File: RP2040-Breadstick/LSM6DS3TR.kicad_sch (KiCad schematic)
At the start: 2 parts, among them U401 LSM6DSMTR

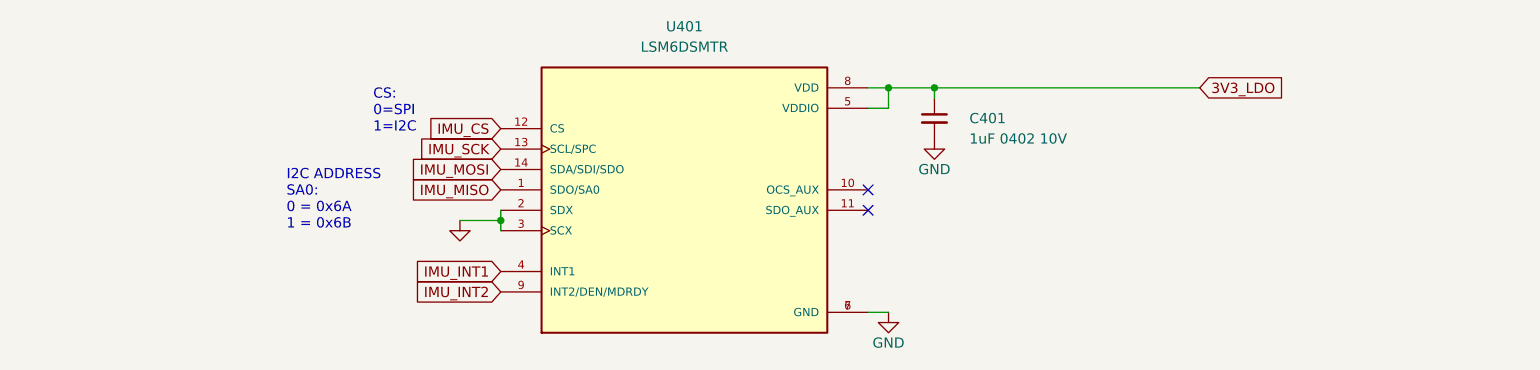
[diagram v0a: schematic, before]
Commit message: Switched IMU to I2C
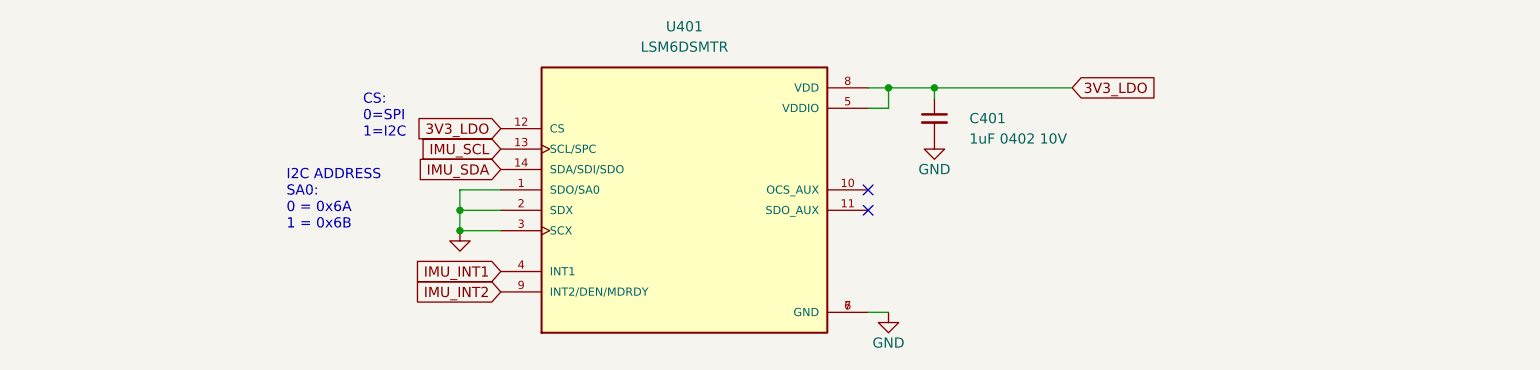
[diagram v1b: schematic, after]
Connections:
- net IMU_CS is gone; now on net 3V3_LDO: U401.12 (CS)
- net IMU_MISO is gone; now on net GND: U401.1 (SDO/SA0)
- net IMU_MOSI renamed IMU_SDA
- net IMU_SCK renamed IMU_SCL
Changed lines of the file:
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@@
   (junction (at 174.625 81.28) (diameter 0) (color 0 0 0 0)
   )
-  (junction (at 126.365 97.79) (diameter 0) (color 0 0 0 0)
+  (junction (at 121.285 99.06) (diameter 0) (color 0 0 0 0)
+  )
+  (junction (at 121.285 96.52) (diameter 0) (color 0 0 0 0)
   )
   (junction (at 180.34 81.28) (diameter 0) (color 0 0 0 0)
@@
     (stroke (width 0) (type default) (color 0 0 0 0))
   )
-  (wire (pts (xy 126.365 96.52) (xy 126.365 97.79))
+  (wire (pts (xy 121.285 93.98) (xy 121.285 96.52))
     (stroke (width 0) (type default) (color 0 0 0 0))
   )
-  (wire (pts (xy 126.365 97.79) (xy 126.365 99.06))
-    (stroke (width 0) (type default) (color 0 0 0 0))
-  )
-  (wire (pts (xy 180.34 81.28) (xy 213.36 81.28))
+  (wire (pts (xy 180.34 81.28) (xy 197.485 81.28))
     (stroke (width 0) (type default) (color 0 0 0 0))
   )
@@
     (stroke (width 0) (type default) (color 0 0 0 0))
   )
-  (wire (pts (xy 121.285 97.79) (xy 126.365 97.79))
+  (wire (pts (xy 174.625 83.82) (xy 174.625 81.28))
     (stroke (width 0) (type default) (color 0 0 0 0))
   )
-  (wire (pts (xy 174.625 83.82) (xy 174.625 81.28))
+  (wire (pts (xy 126.365 93.98) (xy 121.285 93.98))
     (stroke (width 0) (type default) (color 0 0 0 0))
   )
@@
     (stroke (width 0) (type default) (color 0 0 0 0))
   )
+  (wire (pts (xy 121.285 96.52) (xy 126.365 96.52))
+    (stroke (width 0) (type default) (color 0 0 0 0))
+  )
+  (wire (pts (xy 121.285 96.52) (xy 121.285 99.06))
+    (stroke (width 0) (type default) (color 0 0 0 0))
+  )
+  (wire (pts (xy 121.285 99.06) (xy 126.365 99.06))
+    (stroke (width 0) (type default) (color 0 0 0 0))
+  )
   (text "I2C ADDRESS\nSA0:\n0 = 0x6A\n1 = 0x6B" (at 99.695 99.06 0)
     (effects (font (size 1.27 1.27)) (justify left bottom))
   )
-  (text "CS:\n0=SPI\n1=I2C" (at 110.49 86.995 0)
+  (text "CS:\n0=SPI\n1=I2C" (at 109.22 87.63 0)
     (effects (font (size 1.27 1.27)) (justify left bottom))
   )
-  (global_label "IMU_SCK" (shape input) (at 126.365 88.9 180) (fields_autoplaced)
+  (global_label "IMU_SDA" (shape input) (at 126.365 91.44 180) (fields_autoplaced)
     (effects (font (size 1.27 1.27)) (justify right))
-    (property "Intersheet References" "${INTERSHEET_REFS}" (id 0) (at 115.8481 88.9794 0)
+    (property "Intersheet References" "${INTERSHEET_REFS}" (id 0) (at 116.0295 91.5194 0)
       (effects (font (size 1.27 1.27)) (justify right) hide)
     )
@@
     )
   )
-  (global_label "3V3_LDO" (shape input) (at 213.36 81.28 0) (fields_autoplaced)
+  (global_label "3V3_LDO" (shape input) (at 197.485 81.28 0) (fields_autoplaced)
     (effects (font (size 1.27 1.27)) (justify left))
-    (property "Intersheet References" "${INTERSHEET_REFS}" (id 0) (at 223.8769 81.2006 0)
+    (property "Intersheet References" "${INTERSHEET_REFS}" (id 0) (at 208.0019 81.2006 0)
       (effects (font (size 1.27 1.27)) (justify left) hide)
     )
@@
     )
   )
-  (global_label "IMU_CS" (shape input) (at 126.365 86.36 180) (fields_autoplaced)
+  (global_label "3V3_LDO" (shape input) (at 126.365 86.36 180) (fields_autoplaced)
     (effects (font (size 1.27 1.27)) (justify right))
-    (property "Intersheet References" "${INTERSHEET_REFS}" (id 0) (at 117.1181 86.4394 0)
+    (property "Intersheet References" "${INTERSHEET_REFS}" (id 0) (at 115.8481 86.4394 0)
       (effects (font (size 1.27 1.27)) (justify right) hide)
     )
   )
-  (global_label "IMU_MOSI" (shape input) (at 126.365 91.44 180) (fields_autoplaced)
+  (global_label "IMU_SCL" (shape input) (at 126.365 88.9 180) (fields_autoplaced)
     (effects (font (size 1.27 1.27)) (justify right))
-    (property "Intersheet References" "${INTERSHEET_REFS}" (id 0) (at 115.0014 91.5194 0)
-      (effects (font (size 1.27 1.27)) (justify right) hide)
-    )
-  )
-  (global_label "IMU_MISO" (shape input) (at 126.365 93.98 180) (fields_autoplaced)
-    (effects (font (size 1.27 1.27)) (justify right))
-    (property "Intersheet References" "${INTERSHEET_REFS}" (id 0) (at 115.0014 94.0594 0)
+    (property "Intersheet References" "${INTERSHEET_REFS}" (id 0) (at 116.09 88.9794 0)
       (effects (font (size 1.27 1.27)) (justify right) hide)
     )
@@
     (pin "1")
   )
-  (symbol (lib_id "power:GND") (at 121.285 97.79 0) (unit 1)
+  (symbol (lib_id "power:GND") (at 121.285 99.06 0) (unit 1)
     (in_bom yes) (on_board yes)
-    (property "Reference" "#PWR0401" (id 0) (at 121.285 104.14 0)
+    (property "Reference" "#PWR0401" (id 0) (at 121.285 105.41 0)
       (effects (font (size 1.27 1.27)) hide)
     )
-    (property "Value" "~" (id 1) (at 121.285 101.6 0))
-    (property "Footprint" "" (id 2) (at 121.285 97.79 0)
+    (property "Value" "~" (id 1) (at 121.285 102.87 0))
+    (property "Footprint" "" (id 2) (at 121.285 99.06 0)
       (effects (font (size 1.27 1.27)) hide)
     )
-    (property "Datasheet" "" (id 3) (at 121.285 97.79 0)
+    (property "Datasheet" "" (id 3) (at 121.285 99.06 0)
       (effects (font (size 1.27 1.27)) hide)
     )

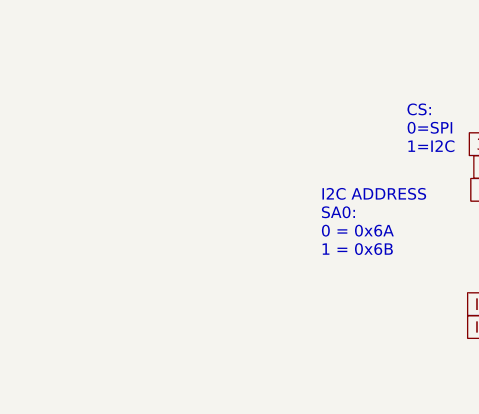
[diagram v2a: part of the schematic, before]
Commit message: Working on several issues simultaneously from the schematic side.
Added hierarchical connections between schematic sheets.
Added ideal ORing diodes.
Unstacked Pins and Added internal diagrams to: USB connector, TVS Diodes, ORing Diodes, LDO, RP2040, etc.
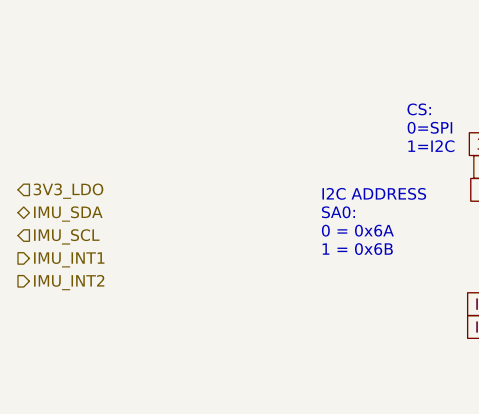
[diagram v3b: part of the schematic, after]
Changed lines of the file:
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@@
     )
+  )
+  (hierarchical_label "IMU_SCL" (shape input) (at 66.04 96.52 0)
+    (effects (font (size 1.27 1.27)) (justify left))
+  )
+  (hierarchical_label "IMU_INT2" (shape output) (at 66.04 101.6 0)
+    (effects (font (size 1.27 1.27)) (justify left))
+  )
+  (hierarchical_label "3V3_LDO" (shape input) (at 66.04 91.44 0)
+    (effects (font (size 1.27 1.27)) (justify left))
+  )
+  (hierarchical_label "IMU_SDA" (shape bidirectional) (at 66.04 93.98 0)
+    (effects (font (size 1.27 1.27)) (justify left))
+  )
+  (hierarchical_label "IMU_INT1" (shape output) (at 66.04 99.06 0)
+    (effects (font (size 1.27 1.27)) (justify left))
   )
   (symbol (lib_id "Device:C_Small") (at 180.34 85.09 0) (mirror y) (unit 1)

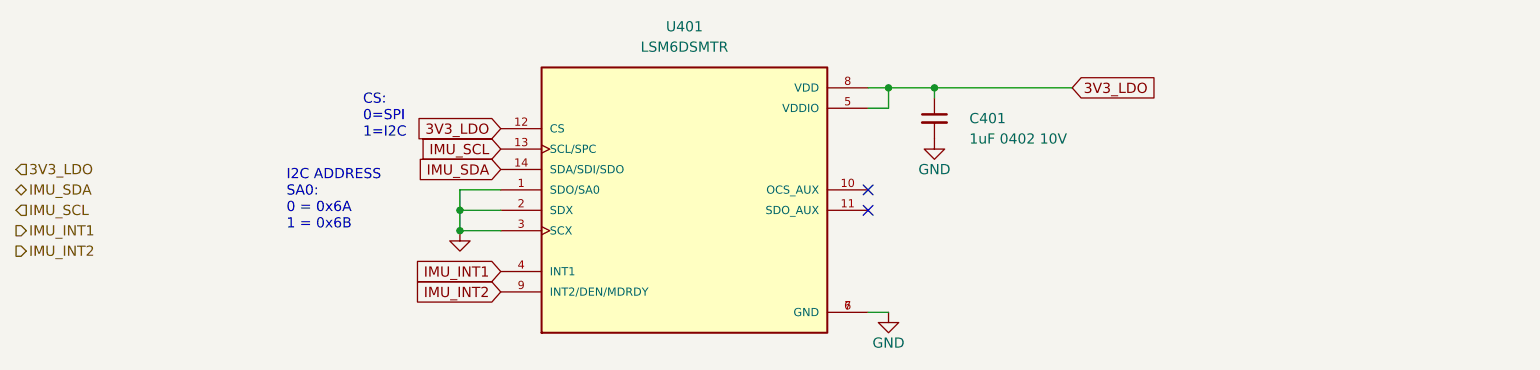
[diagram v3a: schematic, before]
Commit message: Continued cleaning up schematic
Finished most of the microcontroller sheet.
Added hierarchical pins to LED and IMU sheets.
Replaced 24 caps for the LEDs with 6 1206 caps.
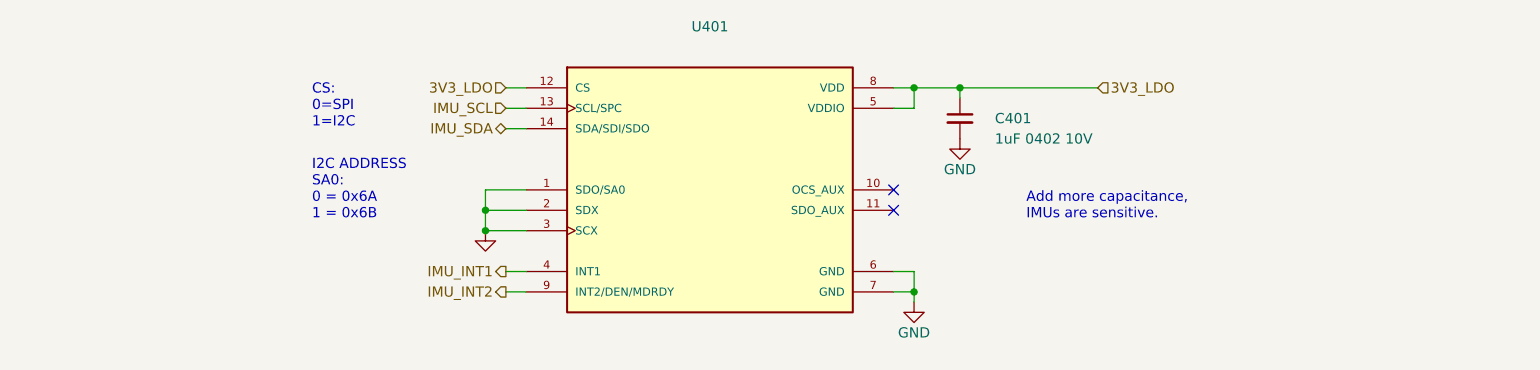
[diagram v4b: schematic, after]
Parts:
- U401: value LSM6DSMTR -> (none); footprint LSM6DSMTR:PQFN50P300X250X86-14N -> PQFN50P300X250X86-14N
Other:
- note added: "Add more capacitance, IMUs are sensitive."
- moved on the sheet: C401

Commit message: Moved schematic changes into PCB
All the changes made in the schematic have been moved into the PCB editor. It was a bit of work due to the amount of reorganizing done in the schematic which led to a lot of new reference numbers. Was easy enough to get most things back into place where they were before.
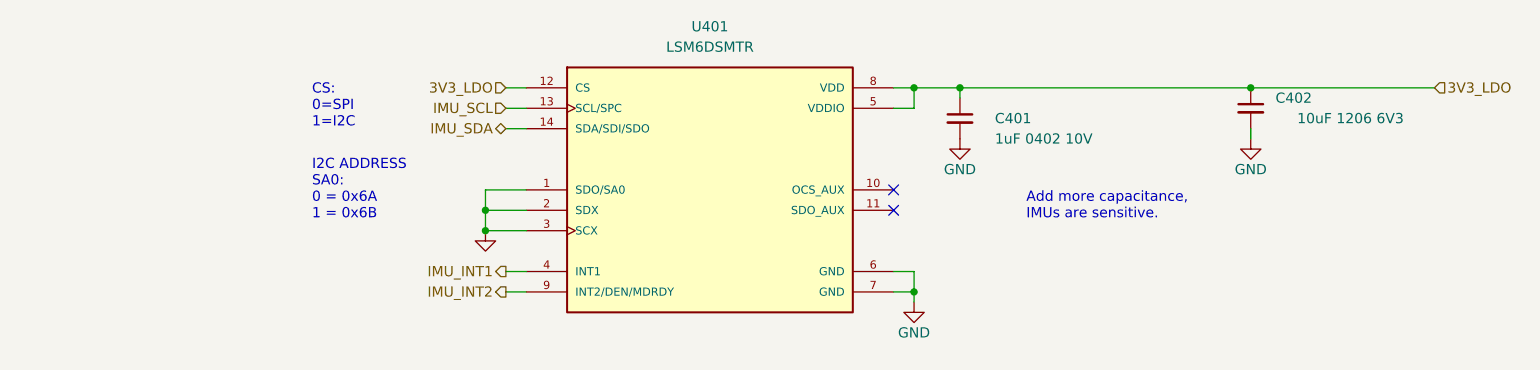
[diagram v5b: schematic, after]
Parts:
- added C402: 10uF 1206 6V3, Capacitor_SMD:C_1206_3216Metric, symbol Device:C_Small
- U401: value (none) -> LSM6DSMTR
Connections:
- net 3V3_LDO: now also C402.1
- net GND: now also C402.2
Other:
- title: RP2040 Breadstick -> Raspberry Breadstick
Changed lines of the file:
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@@
   (paper "A4")
   (title_block
-    (title "RP2040 Breadstick")
-    (date "2023-02-27")
-    (rev "0.1")
+    (title "Raspberry Breadstick")
+    (date "2023-07-02")
+    (rev "0.2")
     (company "J & R Creative Technologies Inc.")
     (comment 1 "@RangenMichael")
     (comment 2 "https://twitter.com/RangenMichael")
     (comment 3 "Apache-2.0 License")
-    (comment 4 "https://github.com/mrangen/RP2040-Breadstick")
+    (comment 4 "https://github.com/mrangen/Raspberry-Breadstick")
+    (comment 5 "https://shop.breadstick.ca/")
+  )
+  (junction (at 219.71 81.28) (diameter 0) (color 0 0 0 0)
   )
   (junction (at 177.8 106.68) (diameter 0) (color 0 0 0 0)
@@
     (stroke (width 0) (type default) (color 0 0 0 0))
   )
-  (wire (pts (xy 183.515 81.28) (xy 200.66 81.28))
+  (wire (pts (xy 183.515 81.28) (xy 219.71 81.28))
     (stroke (width 0) (type default) (color 0 0 0 0))
   )
@@
     (stroke (width 0) (type default) (color 0 0 0 0))
   )
+  (wire (pts (xy 219.71 86.36) (xy 219.71 87.63))
+    (stroke (width 0) (type default) (color 0 0 0 0))
+  )
   (wire (pts (xy 175.26 81.28) (xy 177.8 81.28))
+    (stroke (width 0) (type default) (color 0 0 0 0))
+  )
+  (wire (pts (xy 219.71 81.28) (xy 242.57 81.28))
     (stroke (width 0) (type default) (color 0 0 0 0))
   )
@@
     (effects (font (size 1.27 1.27)) (justify right))
   )
-  (hierarchical_label "3V3_LDO" (shape input) (at 200.66 81.28 0)
+  (hierarchical_label "3V3_LDO" (shape input) (at 242.57 81.28 0)
     (effects (font (size 1.27 1.27)) (justify left))
   )
@@
     )
     (property "Digikey" "1276-1076-6-ND" (id 5) (at 183.515 85.09 0)
+      (effects (font (size 1.27 1.27)) hide)
+    )
+    (pin "1")
+    (pin "2")
+  )
+  (symbol (lib_id "Device:C_Small") (at 219.71 83.82 0) (mirror y) (unit 1)
+    (in_bom yes) (on_board yes)
+    (property "Reference" "C402" (id 0) (at 227.33 82.55 0)
+      (effects (font (size 1.27 1.27)) (justify left))
+    )
+    (property "Value" "10uF 1206 6V3" (id 1) (at 238.76 85.09 0)
+      (effects (font (size 1.27 1.27)) (justify left))
+    )
+    (property "Footprint" "Capacitor_SMD:C_1206_3216Metric" (id 2) (at 219.71 83.82 0)
+      (effects (font (size 1.27 1.27)) hide)
+    )
+    (property "Datasheet" "~" (id 3) (at 219.71 83.82 0)
+      (effects (font (size 1.27 1.27)) hide)
+    )
+    (property "JLCPCB P/N" "" (id 4) (at 219.71 83.82 0)
+      (effects (font (size 1.27 1.27)) hide)
+    )
+    (property "Digikey" "1276-1134-6-ND" (id 5) (at 219.71 83.82 0)
       (effects (font (size 1.27 1.27)) hide)
     )
@@
     )
     (property "Datasheet" "" (id 3) (at 183.515 87.63 0)
+      (effects (font (size 1.27 1.27)) hide)
+    )
+    (pin "1")
+  )
+  (symbol (lib_id "power:GND") (at 219.71 87.63 0) (mirror y) (unit 1)
+    (in_bom yes) (on_board yes)
+    (property "Reference" "#PWR0404" (id 0) (at 219.71 93.98 0)
+      (effects (font (size 1.27 1.27)) hide)
+    )
+    (property "Value" "GND" (id 1) (at 219.71 91.44 0))
+    (property "Footprint" "" (id 2) (at 219.71 87.63 0)
+      (effects (font (size 1.27 1.27)) hide)
+    )
+    (property "Datasheet" "" (id 3) (at 219.71 87.63 0)
       (effects (font (size 1.27 1.27)) hide)
     )
@@
     (in_bom yes) (on_board yes) (fields_autoplaced)
     (property "Reference" "U401" (id 0) (at 152.4 73.66 0))
-    (property "Value" "" (id 1) (at 152.4 76.2 0))
+    (property "Value" "LSM6DSMTR" (id 1) (at 152.4 76.2 0))
     (property "Footprint" "PQFN50P300X250X86-14N" (id 2) (at 152.4 93.98 0)
       (effects (font (size 1.27 1.27)) (justify bottom) hide)

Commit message: working on rev0.2 still
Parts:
- removed C401: 1uF 0402 10V, _Breadstick_Footprints:Perfect_0402_Cap, symbol Device:C_Small
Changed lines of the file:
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@@
   (junction (at 124.46 96.52) (diameter 0) (color 0 0 0 0)
-  )
-  (junction (at 183.515 81.28) (diameter 0) (color 0 0 0 0)
   )
   (no_connect (at 175.26 96.52))
@@
     (stroke (width 0) (type default) (color 0 0 0 0))
   )
-  (wire (pts (xy 183.515 81.28) (xy 219.71 81.28))
-    (stroke (width 0) (type default) (color 0 0 0 0))
-  )
   (wire (pts (xy 127 104.14) (xy 129.54 104.14))
-    (stroke (width 0) (type default) (color 0 0 0 0))
-  )
-  (wire (pts (xy 183.515 81.28) (xy 183.515 82.55))
     (stroke (width 0) (type default) (color 0 0 0 0))
   )
@@
     (stroke (width 0) (type default) (color 0 0 0 0))
   )
-  (wire (pts (xy 177.8 81.28) (xy 183.515 81.28))
+  (wire (pts (xy 177.8 81.28) (xy 219.71 81.28))
     (stroke (width 0) (type default) (color 0 0 0 0))
   )
@@
     (effects (font (size 1.27 1.27)) (justify right))
   )
-  (symbol (lib_id "Device:C_Small") (at 183.515 85.09 0) (mirror y) (unit 1)
-    (in_bom yes) (on_board yes)
-    (property "Reference" "C401" (id 0) (at 192.405 85.09 0)
-      (effects (font (size 1.27 1.27)) (justify left))
-    )
-    (property "Value" "1uF 0402 10V" (id 1) (at 200.025 87.63 0)
-      (effects (font (size 1.27 1.27)) (justify left))
-    )
-    (property "Footprint" "_Breadstick_Footprints:Perfect_0402_Cap" (id 2) (at 183.515 85.09 0)
-      (effects (font (size 1.27 1.27)) hide)
-    )
-    (property "Datasheet" "~" (id 3) (at 183.515 85.09 0)
-      (effects (font (size 1.27 1.27)) hide)
-    )
-    (property "JLCPCB P/N" "" (id 4) (at 183.515 85.09 0)
-      (effects (font (size 1.27 1.27)) hide)
-    )
-    (property "Digikey" "1276-1076-6-ND" (id 5) (at 183.515 85.09 0)
-      (effects (font (size 1.27 1.27)) hide)
-    )
-    (pin "1")
-    (pin "2")
-  )
   (symbol (lib_id "Device:C_Small") (at 219.71 83.82 0) (mirror y) (unit 1)
     (in_bom yes) (on_board yes)
@@
     (pin "2")
   )
-  (symbol (lib_id "power:GND") (at 183.515 87.63 0) (unit 1)
-    (in_bom yes) (on_board yes)
-    (property "Reference" "#PWR0403" (id 0) (at 183.515 93.98 0)
-      (effects (font (size 1.27 1.27)) hide)
-    )
-    (property "Value" "GND" (id 1) (at 183.515 91.44 0))
-    (property "Footprint" "" (id 2) (at 183.515 87.63 0)
-      (effects (font (size 1.27 1.27)) hide)
-    )
-    (property "Datasheet" "" (id 3) (at 183.515 87.63 0)
-      (effects (font (size 1.27 1.27)) hide)
-    )
-    (pin "1")
-  )
   (symbol (lib_id "power:GND") (at 219.71 87.63 0) (mirror y) (unit 1)

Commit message: Updated BOM
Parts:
- C402: value 10uF 1206 6V3 -> (none); footprint Capacitor_SMD:C_1206_3216Metric -> (none)
- U401: value LSM6DSMTR -> (none); footprint PQFN50P300X250X86-14N -> (none); Manufacturer (none) -> STMicroelectronics; Manufacturer_Part_Number (none) -> LSM6DSMTR; Mouser (none) -> 511-LSM6DSMTR; Package (none) -> 14-LGA (2.5x3)
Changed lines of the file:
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@@
       (effects (font (size 1.27 1.27)) (justify left))
     )
-    (property "Value" "10uF 1206 6V3" (id 1) (at 238.76 85.09 0)
+    (property "Value" "" (id 1) (at 238.76 85.09 0)
       (effects (font (size 1.27 1.27)) (justify left))
     )
-    (property "Footprint" "Capacitor_SMD:C_1206_3216Metric" (id 2) (at 219.71 83.82 0)
+    (property "Footprint" "" (id 2) (at 219.71 83.82 0)
       (effects (font (size 1.27 1.27)) hide)
     )
@@
     (in_bom yes) (on_board yes) (fields_autoplaced)
     (property "Reference" "U401" (id 0) (at 152.4 73.66 0))
-    (property "Value" "LSM6DSMTR" (id 1) (at 152.4 76.2 0))
-    (property "Footprint" "PQFN50P300X250X86-14N" (id 2) (at 152.4 93.98 0)
+    (property "Value" "" (id 1) (at 152.4 76.2 0))
+    (property "Footprint" "" (id 2) (at 152.4 93.98 0)
       (effects (font (size 1.27 1.27)) (justify bottom) hide)
     )
@@
       (effects (font (size 1.27 1.27)) hide)
     )
+    (property "Manufacturer" "STMicroelectronics" (id 9) (at 152.4 93.98 0)
+      (effects (font (size 1.27 1.27)) hide)
+    )
+    (property "Manufacturer_Part_Number" "LSM6DSMTR" (id 10) (at 152.4 93.98 0)
+      (effects (font (size 1.27 1.27)) hide)
+    )
+    (property "Package" "14-LGA (2.5x3)" (id 11) (at 152.4 93.98 0)
+      (effects (font (size 1.27 1.27)) hide)
+    )
+    (property "Mouser" "511-LSM6DSMTR" (id 12) (at 152.4 93.98 0)
+      (effects (font (size 1.27 1.27)) hide)
+    )

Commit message: Continued fleshing out the BOM
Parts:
- C402: Manufacturer (none) -> Samsung Electro-Mechanics; Manufacturer_Part_Number (none) -> CL10B225KP8NNNC; Mouser (none) -> 187-CL10B225KP8NNNC; Package (none) -> 1206
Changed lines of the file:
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@@
+      (effects (font (size 1.27 1.27)) hide)
+    )
+    (property "Manufacturer" "Samsung Electro-Mechanics" (id 6) (at 219.71 83.82 0)
+      (effects (font (size 1.27 1.27)) hide)
+    )
+    (property "Manufacturer_Part_Number" "CL10B225KP8NNNC" (id 7) (at 219.71 83.82 0)
+      (effects (font (size 1.27 1.27)) hide)
+    )
+    (property "Mouser" "187-CL10B225KP8NNNC" (id 8) (at 219.71 83.82 0)
+      (effects (font (size 1.27 1.27)) hide)
+    )
+    (property "Package" "1206" (id 9) (at 219.71 83.82 0)
       (effects (font (size 1.27 1.27)) hide)
     )
